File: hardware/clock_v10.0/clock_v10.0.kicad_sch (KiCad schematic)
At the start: 225 parts, among them J1 RJ45, J14 DC-005B-2.5A-2.0, J2 Conn_01x03, J4 USB_C_Receptacle, J5 Conn_01x06_Pin, J6 Conn_01x03_Pin, J8 Conn_01x02_Pin, Q1 2N7002, Q10 2N7002, Q9 2N7002, SW1 SW_Push_4PDT, U1 ADA4807-1, U10 STM32F405RGTx, U11 AMS1117-3.3, U12 BA50DD0WHFP-TR, U13 M24C02-RMN, U14 CH340C, U15 USBLC6-2P6, U16 TLV3603DCKR, U17 SN74LVC1G14DBV, U18 TMP112AIDRLR, U19 SN74LVC1G14DBV, U2 SN74LVC1G14DBV, U20 SN74LVC1G14DBV, U21 SN74LVC1G14DBV, U23 TPS63060, U3 SN74LVC1G14DBV, U4 ADA4807-1, U5 ADA4807-1, U6 TLV3603DCKR, U7 SN74LVC1G14DBV, U8 TLV3603DCKR, U9 L78L05_SOT89, Y1 AOCJY4A-10.000MHZ-SW, Y2 16MHz

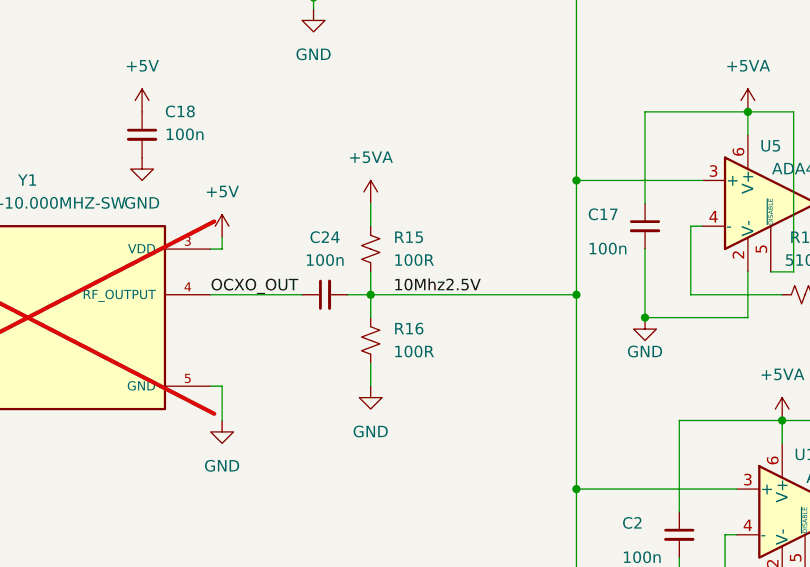
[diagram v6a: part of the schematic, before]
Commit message: moved to 250mW resisotrs. Fixes #289
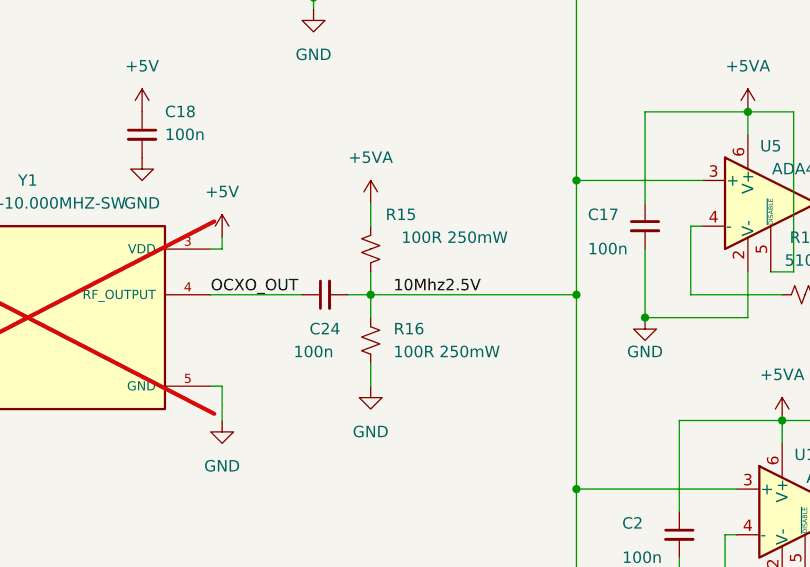
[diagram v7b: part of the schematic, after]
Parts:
- R15, R16: value 100R -> 100R 250mW; footprint Resistor_SMD:R_0603_1608Metric -> Resistor_SMD:R_1206_3216Metric; JLCPCB Part # C22775 -> C17901
- Y1: footprint XTAL_AOCJY4A-10.000MHZ-SW -> blinky_footprints:XTAL_AOCJY4A-10.000MHZ-SW
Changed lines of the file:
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@@
       (effects (font (size 1.27 1.27)))
     )
-    (property "Footprint" "XTAL_AOCJY4A-10.000MHZ-SW" (at 243.84 158.75 0)
+    (property "Footprint" "blinky_footprints:XTAL_AOCJY4A-10.000MHZ-SW" (at 243.84 158.75 0)
       (effects (font (size 1.27 1.27)) (justify bottom) hide)
     )
@@
   )
   (symbol (lib_id "Device:C_Small") (at 276.86 156.21 90) (unit 1)
-    (in_bom yes) (on_board yes) (dnp no) (fields_autoplaced)
-    (property "Reference" "C24" (at 276.8663 149.86 90)
+    (in_bom yes) (on_board yes) (dnp no)
+    (property "Reference" "C24" (at 276.86 160.02 90)
       (effects (font (size 1.27 1.27)))
     )
-    (property "Value" "100n" (at 276.8663 152.4 90)
+    (property "Value" "100n" (at 275.59 162.56 90)
       (effects (font (size 1.27 1.27)))
     )
@@
       (effects (font (size 1.27 1.27)) (justify left))
     )
-    (property "Value" "100R" (at 284.48 162.56 0)
+    (property "Value" "100R 250mW" (at 284.48 162.56 0)
       (effects (font (size 1.27 1.27)) (justify left))
     )
-    (property "Footprint" "Resistor_SMD:R_0603_1608Metric" (at 281.94 161.29 0)
+    (property "Footprint" "Resistor_SMD:R_1206_3216Metric" (at 281.94 161.29 0)
       (effects (font (size 1.27 1.27)) hide)
     )
@@
       (effects (font (size 1.27 1.27)) hide)
     )
-    (property "JLCPCB Part #" "C22775" (at 281.94 161.29 0)
+    (property "JLCPCB Part #" "C17901" (at 281.94 161.29 0)
       (effects (font (size 1.27 1.27)) hide)
     )
@@
     )
   )
-  (symbol (lib_id "Device:R_Small_US") (at 281.94 151.13 0) (unit 1)
-    (in_bom yes) (on_board yes) (dnp no) (fields_autoplaced)
-    (property "Reference" "R15" (at 284.48 149.86 0)
+  (symbol (lib_id "Device:R_Small_US") (at 281.94 151.13 0) (mirror y) (unit 1)
+    (in_bom yes) (on_board yes) (dnp no)
+    (property "Reference" "R15" (at 287.02 147.32 0)
       (effects (font (size 1.27 1.27)) (justify left))
     )
-    (property "Value" "100R" (at 284.48 152.4 0)
+    (property "Value" "100R 250mW" (at 297.18 149.86 0)
       (effects (font (size 1.27 1.27)) (justify left))
     )
-    (property "Footprint" "Resistor_SMD:R_0603_1608Metric" (at 281.94 151.13 0)
+    (property "Footprint" "Resistor_SMD:R_1206_3216Metric" (at 281.94 151.13 0)
       (effects (font (size 1.27 1.27)) hide)
     )
@@
       (effects (font (size 1.27 1.27)) hide)
     )
-    (property "JLCPCB Part #" "C22775" (at 281.94 151.13 0)
+    (property "JLCPCB Part #" "C17901" (at 281.94 151.13 0)
       (effects (font (size 1.27 1.27)) hide)
     )

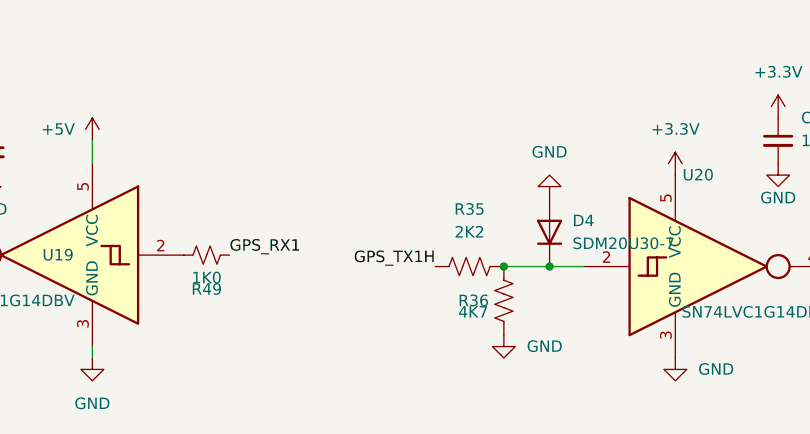
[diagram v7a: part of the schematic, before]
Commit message: fiux voltage dirvide for GPS TX. Fixes #260
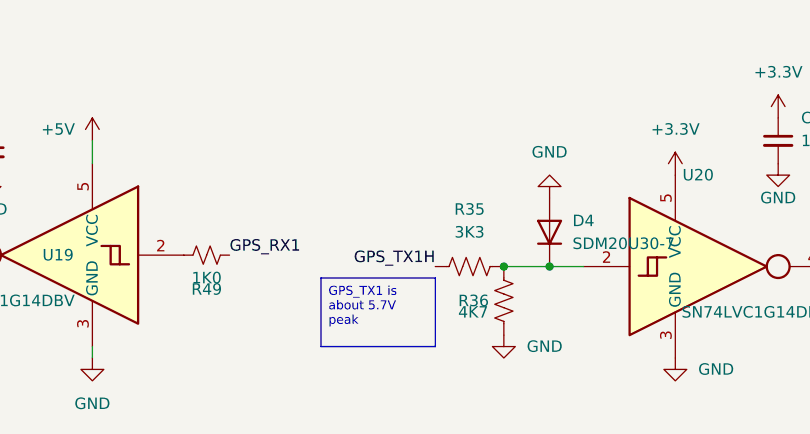
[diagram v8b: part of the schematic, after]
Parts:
- R35: value 2K2 -> 3K3; JLCPCB Part # C4190 -> C22978
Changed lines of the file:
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@@
     (effects (font (size 1 1)) (justify left top))
   )
+  (text_box "GPS_TX1 is about 5.7V peak"
+    (at 351.79 400.05 0) (size 12.7 7.62)
+    (stroke (width 0) (type default))
+    (fill (type none))
+    (effects (font (size 1 1)) (justify left top))
+  )
   (text "At least 16V caps here" (at 133.35 372.11 0)
     (effects (font (size 1 1)) (justify left bottom))
@@
       (effects (font (size 1.27 1.27)))
     )
-    (property "Value" "2K2" (at 368.3 394.97 90)
+    (property "Value" "3K3" (at 368.3 394.97 90)
       (effects (font (size 1.27 1.27)))
     )
@@
       (effects (font (size 1.27 1.27)) hide)
     )
-    (property "LCSC" "" (at 368.3 398.78 0)
-      (effects (font (size 1.27 1.27)) hide)
-    )
-    (property "JLCPCB Part #" "C4190" (at 368.3 398.78 0)
+    (property "JLCPCB Part #" "C22978" (at 368.3 398.78 0)
       (effects (font (size 1.27 1.27)) hide)
     )
